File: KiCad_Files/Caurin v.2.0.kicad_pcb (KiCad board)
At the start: 4 copper layers, 86 x 86 mm, 73 parts, among them IC1 L7806ABD2T-TR, J1 ESQ-120-39-G-D, J2 Conn_01x12_Male, J3 Conn_01x09_Male, J4 CONSMA001-SMD-G, J5 CONSMA001-SMD-G, J6 U_FL-R-SMT_10_, J7 CONSMA001-SMD-G, J8 MEM2075-00-140-01-A, J9 Conn_01x02_Male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

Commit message: Update 7806 Traces
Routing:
- net GND: track 90.3 -> 120.2 mm
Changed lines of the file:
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@@
     (thickness 1.6)
     (drawings 422)
-    (tracks 1233)
+    (tracks 1237)
     (zones 0)
     (modules 73)
@@
   )
   (setup
-    (last_trace_width 0.5)
+    (last_trace_width 1.5)
     (user_trace_width 0.2)
     (user_trace_width 0.25)
@@
     (add_net UART_TX)
   )
+  (module Crystal:Crystal_SMD_3215-2Pin_3.2x1.5mm (layer F.Cu)
+    (at 165.5064 77.89672 180)
+    (descr "SMD Crystal FC-135 https://support.epson.biz/td/api/doc_check.php?dl=brief_FC-135R_en.pdf")
+    (tags "SMD SMT Crystal")
+    (attr smd)
+    (fp_text reference Y1 (at 0 -2.11328) (layer F.SilkS) hide
+      (effects (font (size 1 1) (thickness 0.15)))
+    )
+    (fp_text value 32,768k (at 0 2) (layer F.Fab)
+      (effects (font (size 1 1) (thickness 0.15)))
+    )
+    (fp_line (start 2 -1.15) (end 2 1.15) (layer F.CrtYd) (width 0.05))
+    (fp_line (start -2 -1.15) (end -2 1.15) (layer F.CrtYd) (width 0.05))
+    (fp_line (start -2 1.15) (end 2 1.15) (layer F.CrtYd) (width 0.05))
+    (fp_line (start -1.6 0.75) (end 1.6 0.75) (layer F.Fab) (width 0.1))
+    (fp_line (start -1.6 -0.75) (end 1.6 -0.75) (layer F.Fab) (width 0.1))
+    (fp_line (start 1.6 -0.75) (end 1.6 0.75) (layer F.Fab) (width 0.1))
+    (fp_line (start -0.675 -0.875) (end 0.675 -0.875) (layer F.SilkS) (width 0.12))
+    (fp_line (start -0.675 0.875) (end 0.675 0.875) (layer F.SilkS) (width 0.12))
+    (fp_line (start -1.6 -0.75) (end -1.6 0.75) (layer F.Fab) (width 0.1))
+    (fp_line (start -2 -1.15) (end 2 -1.15) (layer F.CrtYd) (width 0.05))
+    (fp_text user %R (at 0 -2) (layer F.Fab)
+      (effects (font (size 1 1) (thickness 0.15)))
+    )
+    (pad 2 smd rect (at -1.25 0 180) (size 1 1.8) (layers F.Cu F.Paste F.Mask)
+      (net 6 LSE_IN))
+    (pad 1 smd rect (at 1.25 0 180) (size 1 1.8) (layers F.Cu F.Paste F.Mask)
+      (net 7 LSE_OUT))
+    (model ${KISYS3DMOD}/Crystal.3dshapes/Crystal_SMD_MicroCrystal_CC7V-T1A-2Pin_3.2x1.5mm.step
+      (at (xyz 0 0 0))
+      (scale (xyz 1 1 1))
+      (rotate (xyz 0 0 0))
+    )
+  )
   (module RF_Modules_Zenith:2AD66-126x (layer B.Cu)
     (at 143.2664 119.7356 270)
@@
       (effects (font (size 1 1) (thickness 0.15)))
     )
-    (fp_text user %R (at 0 0 180) (layer F.Fab)
-      (effects (font (size 1 1) (thickness 0.15)))
-    )
     (fp_line (start -2.3 -1.6) (end 2.3 -1.6) (layer F.Fab) (width 0.1))
     (fp_line (start 2.3 -1.6) (end 2.5 -1.4) (layer F.Fab) (width 0.1))
@@
     (fp_line (start 2.8 1.9) (end 2.8 -1.9) (layer F.CrtYd) (width 0.05))
     (fp_line (start 2.8 -1.9) (end -2.8 -1.9) (layer F.CrtYd) (width 0.05))
+    (fp_text user %R (at 0 0 180) (layer F.Fab)
+      (effects (font (size 1 1) (thickness 0.15)))
+    )
     (pad 4 smd roundrect (at -1.65 -1 180) (size 2 1.5) (layers F.Cu F.Paste F.Mask) (roundrect_rratio 0.1)
       (net 1 GND))
@@
     )
   )
-  (module Crystal:Crystal_SMD_3215-2Pin_3.2x1.5mm (layer F.Cu)
-    (at 165.5064 77.89672 180)
-    (descr "SMD Crystal FC-135 https://support.epson.biz/td/api/doc_check.php?dl=brief_FC-135R_en.pdf")
-    (tags "SMD SMT Crystal")
-    (attr smd)
-    (fp_text reference Y1 (at 0 -2.11328 180) (layer F.SilkS) hide
-      (effects (font (size 1 1) (thickness 0.15)))
-    )
-    (fp_text value 32,768k (at 0 2 180) (layer F.Fab)
-      (effects (font (size 1 1) (thickness 0.15)))
-    )
-    (fp_line (start 2 -1.15) (end 2 1.15) (layer F.CrtYd) (width 0.05))
-    (fp_line (start -2 -1.15) (end -2 1.15) (layer F.CrtYd) (width 0.05))
-    (fp_line (start -2 1.15) (end 2 1.15) (layer F.CrtYd) (width 0.05))
-    (fp_line (start -1.6 0.75) (end 1.6 0.75) (layer F.Fab) (width 0.1))
-    (fp_line (start -1.6 -0.75) (end 1.6 -0.75) (layer F.Fab) (width 0.1))
-    (fp_line (start 1.6 -0.75) (end 1.6 0.75) (layer F.Fab) (width 0.1))
-    (fp_line (start -0.675 -0.875) (end 0.675 -0.875) (layer F.SilkS) (width 0.12))
-    (fp_line (start -0.675 0.875) (end 0.675 0.875) (layer F.SilkS) (width 0.12))
-    (fp_line (start -1.6 -0.75) (end -1.6 0.75) (layer F.Fab) (width 0.1))
-    (fp_line (start -2 -1.15) (end 2 -1.15) (layer F.CrtYd) (width 0.05))
-    (fp_text user %R (at 0 -2 180) (layer F.Fab)
-      (effects (font (size 1 1) (thickness 0.15)))
-    )
-    (pad 2 smd rect (at -1.25 0 180) (size 1 1.8) (layers F.Cu F.Paste F.Mask)
-      (net 6 LSE_IN))
-    (pad 1 smd rect (at 1.25 0 180) (size 1 1.8) (layers F.Cu F.Paste F.Mask)
-      (net 7 LSE_OUT))
-    (model ${KISYS3DMOD}/Crystal.3dshapes/Crystal_SMD_3215-2Pin_3.2x1.5mm.wrl
-      (at (xyz 0 0 0))
-      (scale (xyz 1 1 1))
-      (rotate (xyz 0 0 0))
-    )
-    (model ${KISYS3DMOD}/Crystal.3dshapes/Crystal_SMD_MicroCrystal_CC7V-T1A-2Pin_3.2x1.5mm.step
-      (at (xyz 0 0 0))
-      (scale (xyz 1 1 1))
-      (rotate (xyz 0 0 0))
-    )
-  )
   (module SamacSys_Parts:YC164JR07220RL (layer B.Cu)
     (at 179.2605 96.0755)
@@
   (via (at 127.3175 120.396) (size 0.8) (drill 0.4) (layers F.Cu B.Cu) (net 1))
   (via (at 128.2065 121.3485) (size 0.8) (drill 0.4) (layers F.Cu B.Cu) (net 1))
+  (segment (start 124.4981 84.9738) (end 124.4981 77.1652) (width 1.5) (layer F.Cu) (net 1))
+  (segment (start 124.4981 84.9738) (end 132.2813 84.9738) (width 1.5) (layer F.Cu) (net 1))
+  (segment (start 124.4981 84.9738) (end 116.3047 84.9738) (width 1.5) (layer F.Cu) (net 1))
+  (segment (start 124.4981 84.9738) (end 124.4981 91.0717) (width 1.5) (layer F.Cu) (net 1))
   (segment (start 154.8384 76.05542) (end 155.2204 75.67342) (width 0.3) (layer F.Cu) (net 2))
   (segment (start 154.8384 77.89672) (end 154.8384 76.05542) (width 0.3) (layer F.Cu) (net 2))

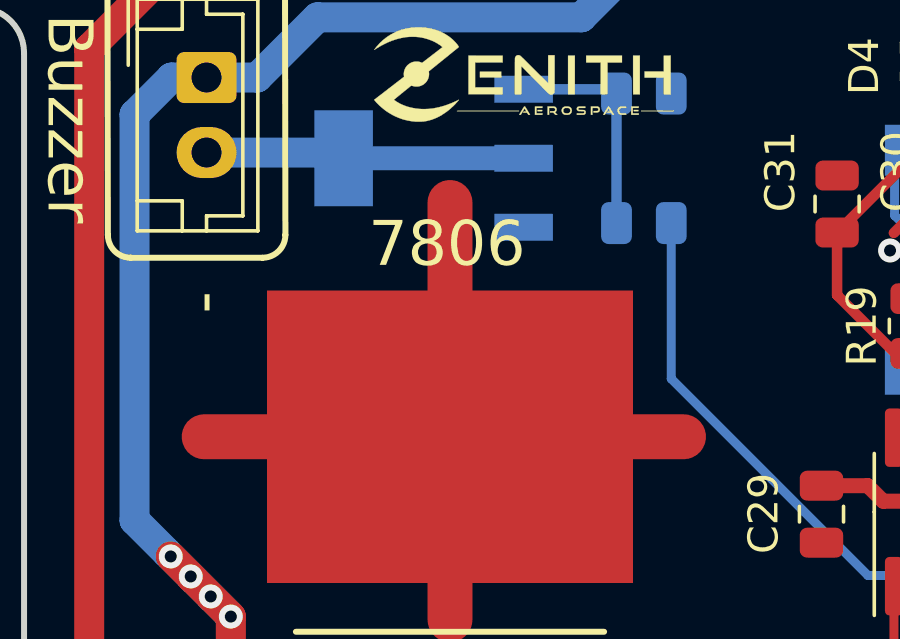
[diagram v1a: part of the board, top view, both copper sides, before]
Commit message: Add shapes3D folder
Now all 3D models for the components are stored in a single folder, thanks to the Archive Plugin from https://github.com/MitjaNemec/Kicad_action_plugins.git
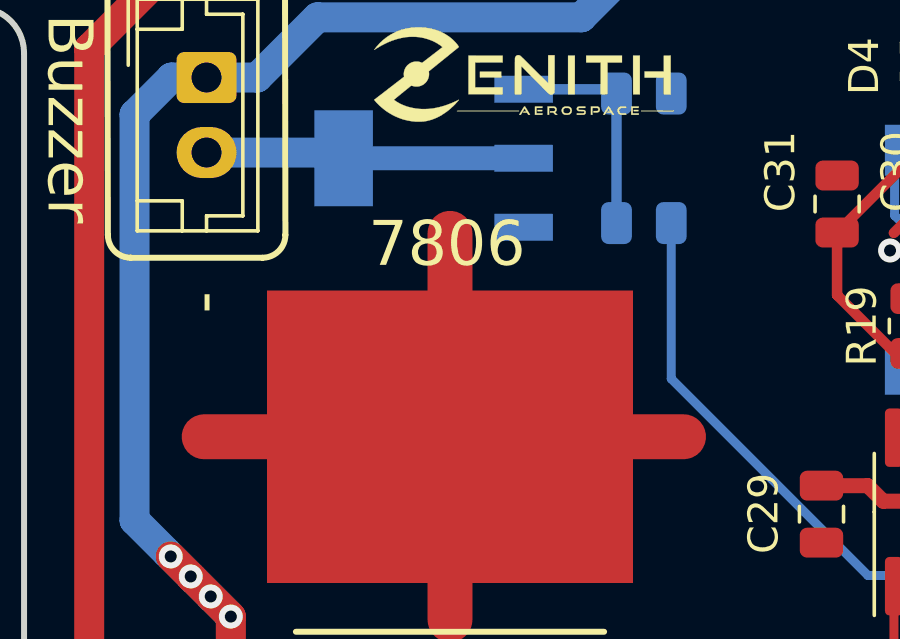
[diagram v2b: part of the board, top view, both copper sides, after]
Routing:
- net GND: track 120.2 -> 119.2 mm

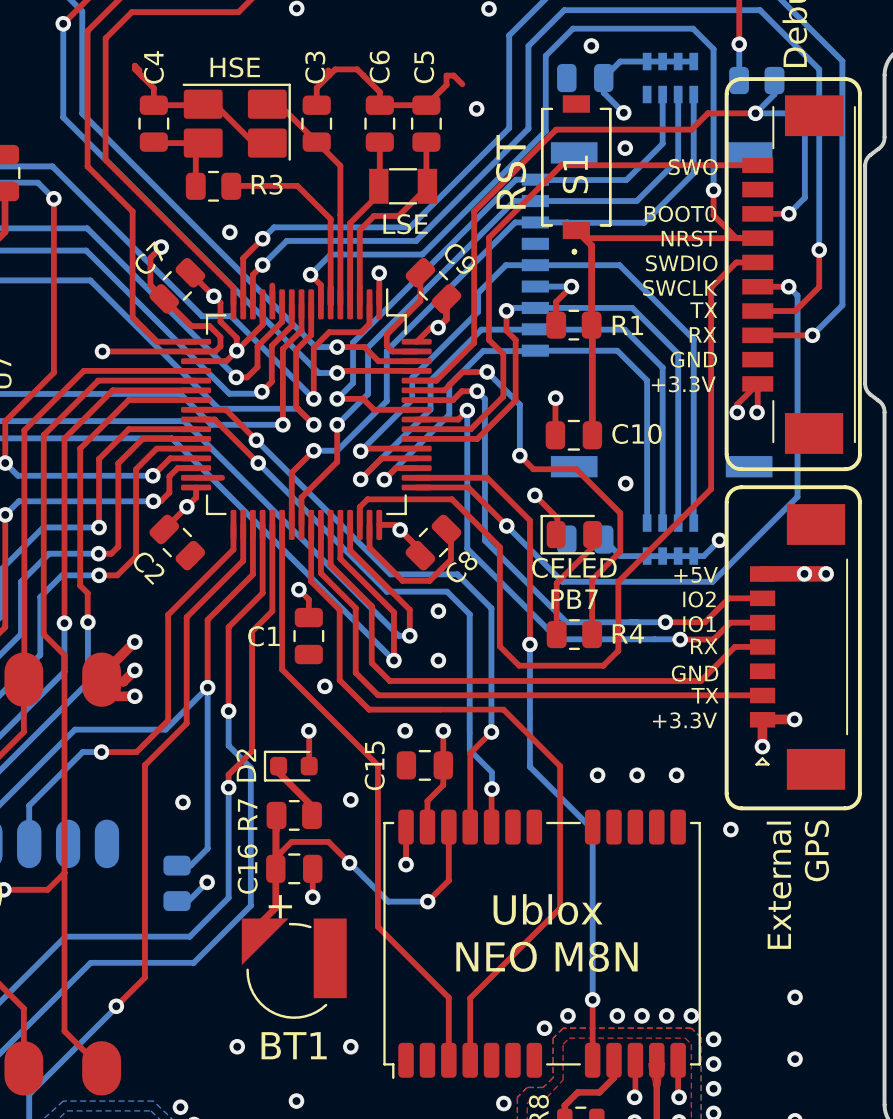
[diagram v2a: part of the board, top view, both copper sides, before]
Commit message: Add RTC backup battery
Add the CR1025 RTC Button Cell Battery. Update schematic images and PDF.
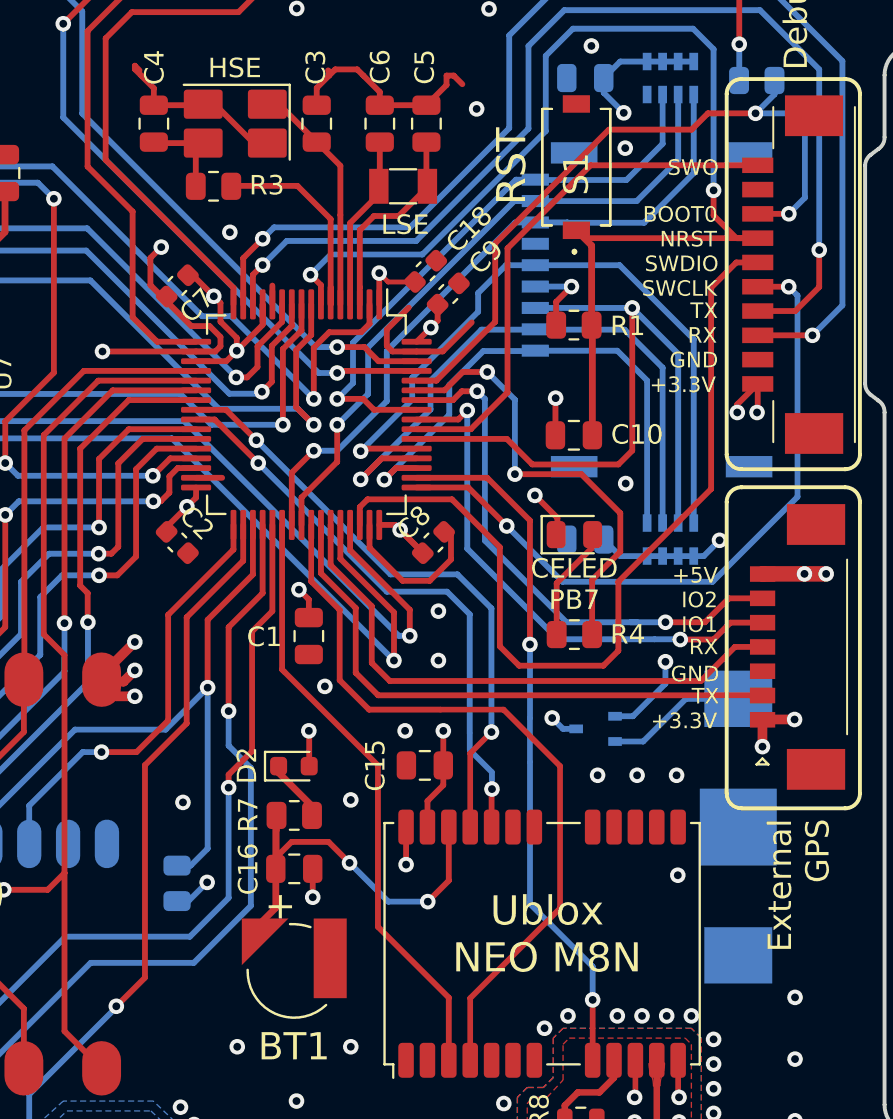
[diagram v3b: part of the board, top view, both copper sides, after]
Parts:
- added BT2: Battery_Cell, SamacSys_Parts:3030, B.Cu at (182.8, 110.9)
- added C18: 100n, Capacitor_SMD:C_0603_1608Metric, F.Cu at (166.7, 82.3)
- added D3: BAT54CW, Package_TO_SOT_SMD:SOT-323_SC-70, B.Cu at (175.4, 105.8)
- C2, C7, C8, C9: footprint Capacitor_SMD:C_0805_2012Metric -> Capacitor_SMD:C_0603_1608Metric
- moved C9 0.87 mm to (167.8, 83.4), turned to 45 degrees
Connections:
- U1 pad 1: 3V3 -> RTC_BAT
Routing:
- net RTC_BAT: track 0.00 -> 31.7 mm, vias 0 -> 2
- net Net-(BT2-Pad1): track 0.00 -> 7.95 mm
- net SD_CARD_CMD: track 29.3 -> 36.3 mm
- net 3V3: track 105.5 -> 107.6 mm
- net BOOT0: track 38.4 -> 36.8 mm
- net SWO: track 29.0 -> 27.5 mm
- net GND: track 119.2 -> 120.2 mm
- net DEBUG_LED: track 22.3 -> 23.0 mm

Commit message: Update RTC Battery silk screen name
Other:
- board text added: "RTC-BAT"

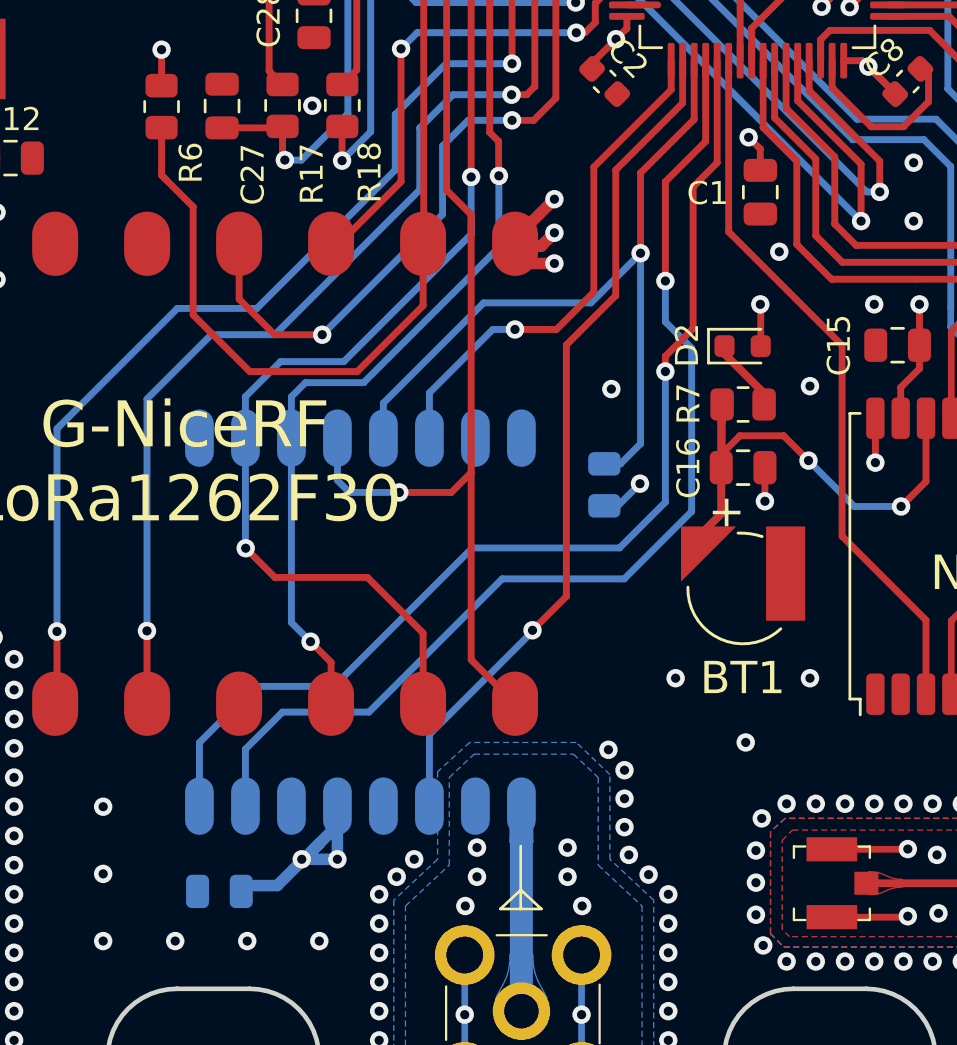
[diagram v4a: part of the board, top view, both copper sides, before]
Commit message: Add solder jumper for DIO pins.
Adds solder jumper for DIO pin compatibility between SX1276 and SX1262 low power radios.
Also added the name of the designer (me).
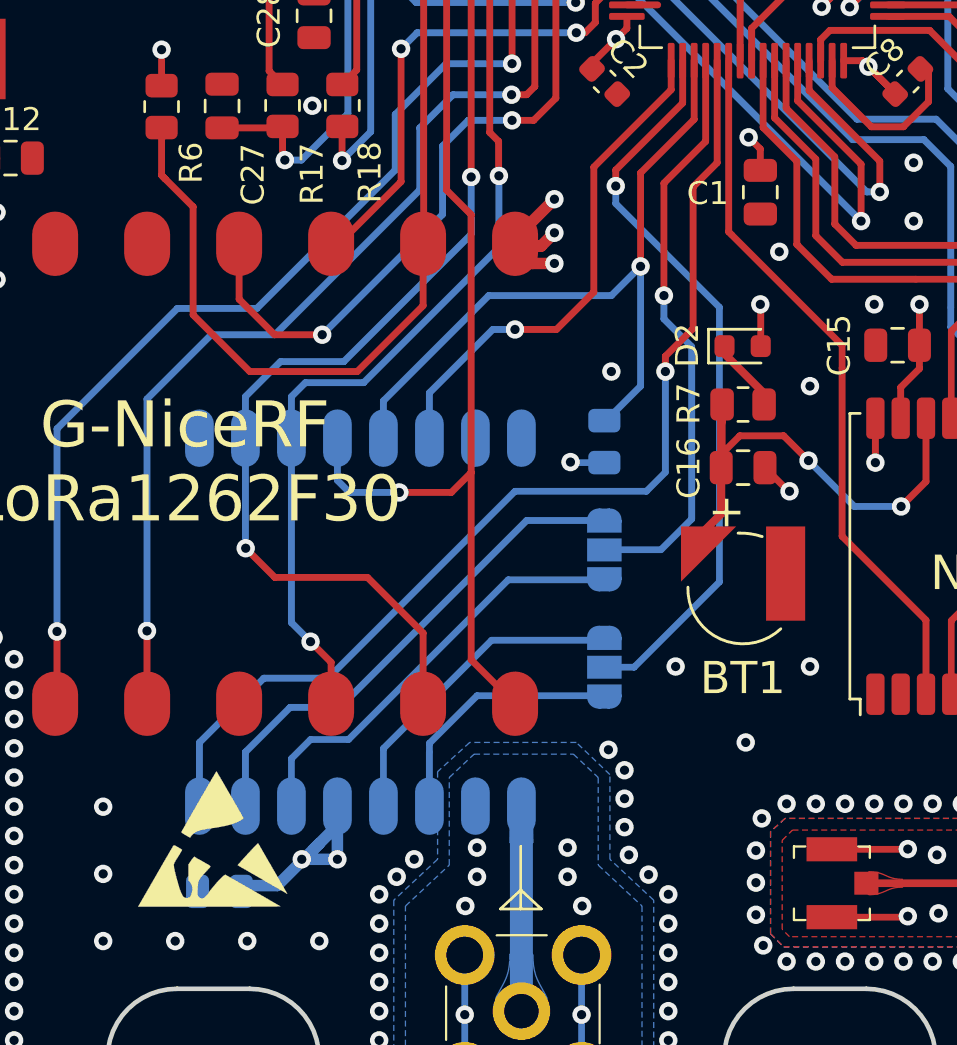
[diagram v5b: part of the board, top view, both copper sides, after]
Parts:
- removed the G*** at (132.8, 98.3)
- added G***: LOGO, LogosZenith:CaurinLogoV2_noyear_7mm, B.Cu at (121.2, 98.7)
- added JP3: SolderJumper_3_Open, Caurin_Footprints:SolderJumper-3_P1.3mm_Open_RoundedPad1.0x1.5mm_NumberLabels, B.Cu at (153.9, 116.6)
- added JP4: SolderJumper_3_Open, Caurin_Footprints:SolderJumper-3_P1.3mm_Open_RoundedPad1.0x1.5mm_NumberLabels, B.Cu at (153.9, 121.7)
- added REF**: ESD-Logo_6.6x6mm_SilkScreen, Symbol:ESD-Logo_6.6x6mm_SilkScreen, F.Cu at (136.8, 129.2)
- moved G*** 8.38 mm to (130.6, 99.1)
- moved R5 1.88 mm to (153.9, 111.9)
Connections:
- U2 pad 1: GND -> Net-(U2-Pad1)
- U2 pad 11: RADIO2_DIO3 -> Net-(JP4-Pad1)
- U2 pad 15: RADIO2_DIO1 -> Net-(JP3-Pad3)
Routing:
- net Net-(JP3-Pad3): track 0.00 -> 22.0 mm
- net RADIO2_DIO1: track 46.7 -> 25.5 mm
- net Net-(JP3-Pad1): track 0.00 -> 18.9 mm
- net Net-(JP4-Pad3): track 0.00 -> 14.1 mm
- net Net-(JP4-Pad1): track 0.00 -> 11.1 mm
- net RADIO2_DIO3: track 36.7 -> 32.3 mm
- net RADIO2_NSS: track 35.5 -> 31.4 mm
- net RADIO2_BUSY: track 47.2 -> 46.5 mm
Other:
- board text added: "DIO0"
- board text added: "DIO1"
- board text added: "DIO3"
- board text added: "DIO4"
- board text added: "Projetista: Júlio Calandrin :)"
- board text added: "github.com/zenitheesc/Probe-CDH"
